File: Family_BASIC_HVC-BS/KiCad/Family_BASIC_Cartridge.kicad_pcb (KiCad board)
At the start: 2 copper layers, 90 x 90 mm, 19 parts, among them IC1 Working RAM (62256), IC2 Program ROM (27256), IC3 74HCT20, IC4 Character ROM (2764), SW1 BACKUP SW, SW2 RAM BANK SW

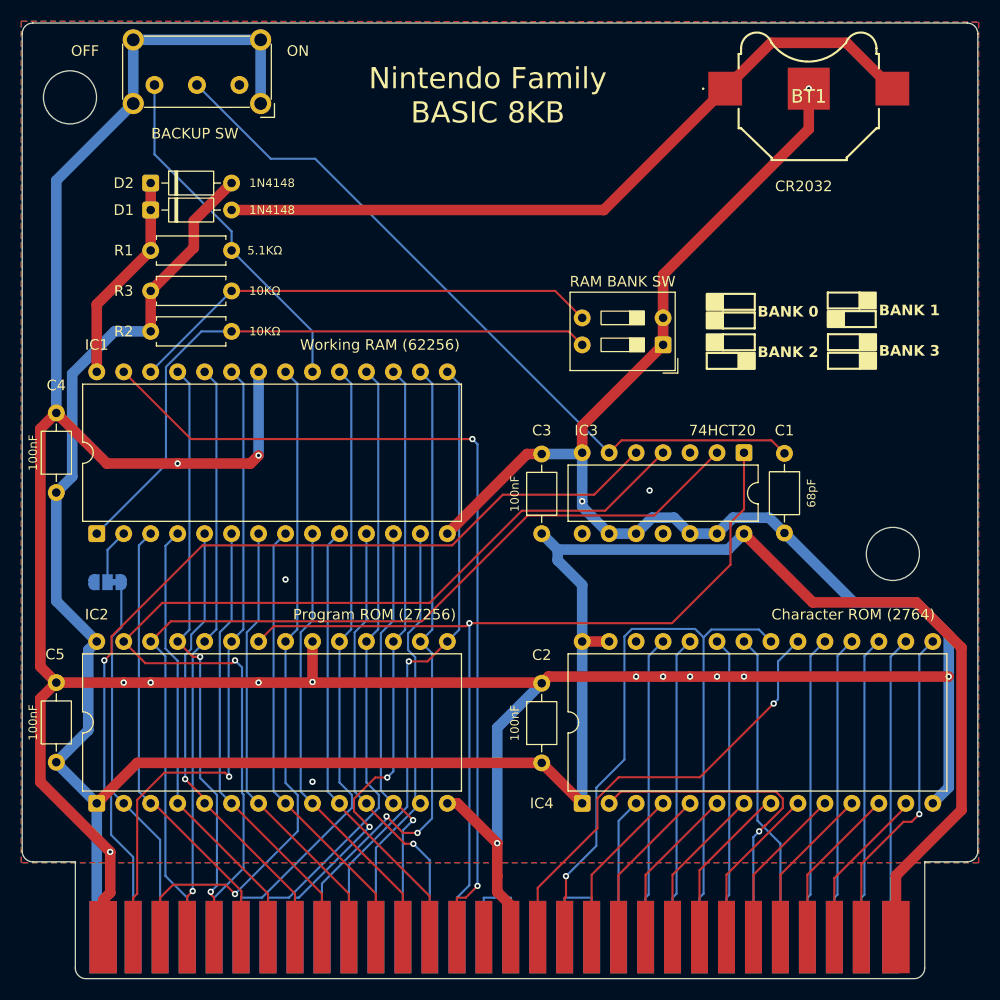
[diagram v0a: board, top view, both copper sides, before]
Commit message: Switched PRG ROM to 27512
Switch between v2.1 and v3.0 Family BASIC
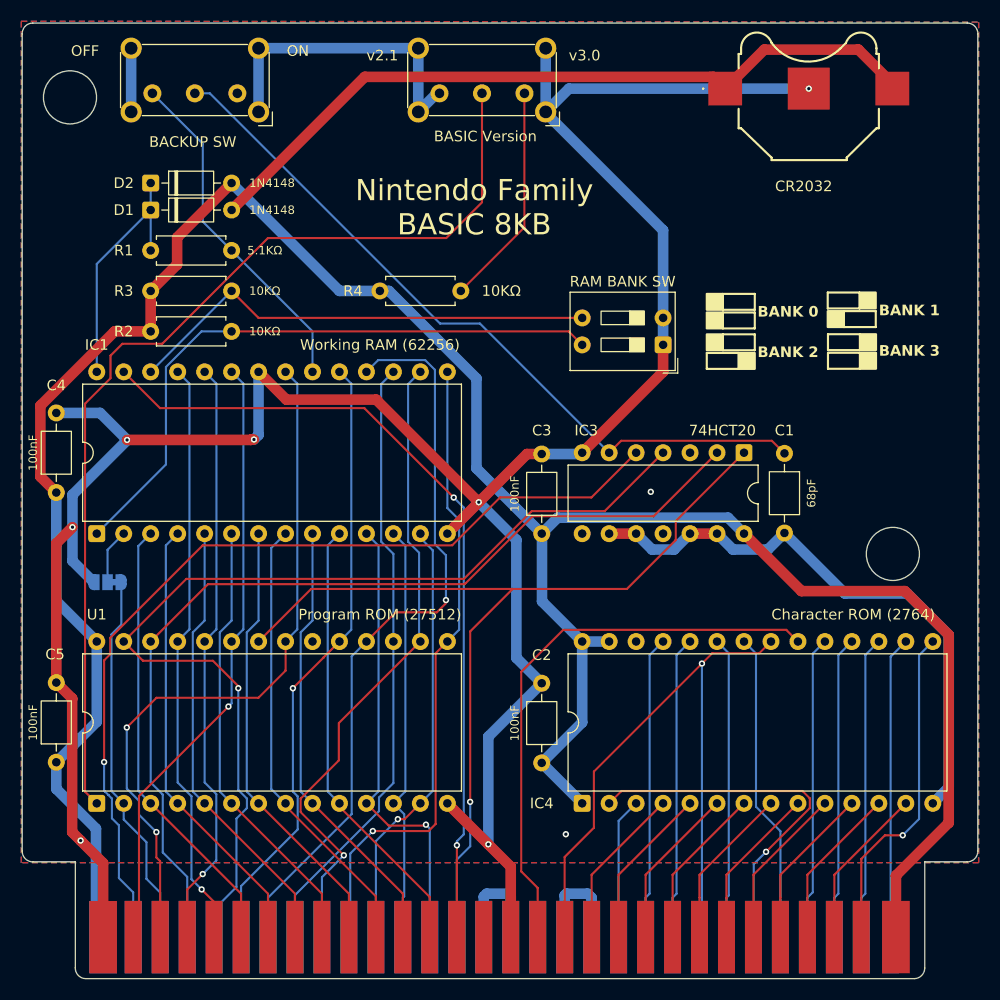
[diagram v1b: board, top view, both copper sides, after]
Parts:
- removed IC2: Program ROM (27256), Package_DIP:DIP-28_W15.24mm
- added R4: 10KΩ, Resistor_THT:R_Axial_DIN0207_L6.3mm_D2.5mm_P7.62mm_Horizontal, F.Cu at (91.8, 82.7)
- added SW3: A_{15} SW, Button_Switch_THT:SW_E-Switch_EG1224_SPDT_Angled, F.Cu at (105.4, 64.1)
- added U1: Program ROM (27512), Package_DIP:DIP-28_W15.24mm, F.Cu at (65.1, 131.0)
- moved SW1 0.81 mm to (78.4, 64.1)
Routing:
- net /A_{15}: track 0.00 -> 94.8 mm
- net /GND: track 382.8 -> 339.4 mm, vias 19 -> 9
- net Net-(SW3-A): track 0.00 -> 21.1 mm
- net /~{RD}: track 42.5 -> 53.8 mm, vias 1 -> 0
- net /D_{6}: track 60.1 -> 70.4 mm, vias 0 -> 1
- net /PA_{10}: track 74.3 -> 64.3 mm
- net /R/~{W}: track 83.9 -> 78.0 mm
- net /V_{CC}: track 236.1 -> 241.7 mm
- net /A_{11}: track 62.1 -> 58.0 mm
- net /RAMV_{CC}: track 19.9 -> 23.7 mm
- net /PA_{12}: track 31.3 -> 34.9 mm
- net /A_{10}: track 64.7 -> 67.3 mm, vias 1 -> 2
- net /D_{3}: track 59.0 -> 61.1 mm
- net /D_{5}: track 60.1 -> 58.0 mm, vias 2 -> 0
- net /D_{7}: track 60.1 -> 58.4 mm, vias 0 -> 1
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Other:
- board text added: "BASIC Version"
- board text added: "v2.1"
- board text added: "v3.0"
